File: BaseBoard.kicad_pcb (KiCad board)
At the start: 2 copper layers, 80 parts, among them U1 TLC5971PWP, U10 TLC5971PWP, U11 TLC5971PWP, U12 TLC5971PWP, U13 TLC5971PWP, U14 TLC5971PWP, U15 TLC5971PWP, U16 TLC5971PWP, U2 TLC5971PWP, U3 TLC5971PWP, U4 TLC5971PWP, U5 TLC5971PWP, U6 TLC5971PWP, U7 TLC5971PWP, U8 TLC5971PWP, U9 TLC5971PWP

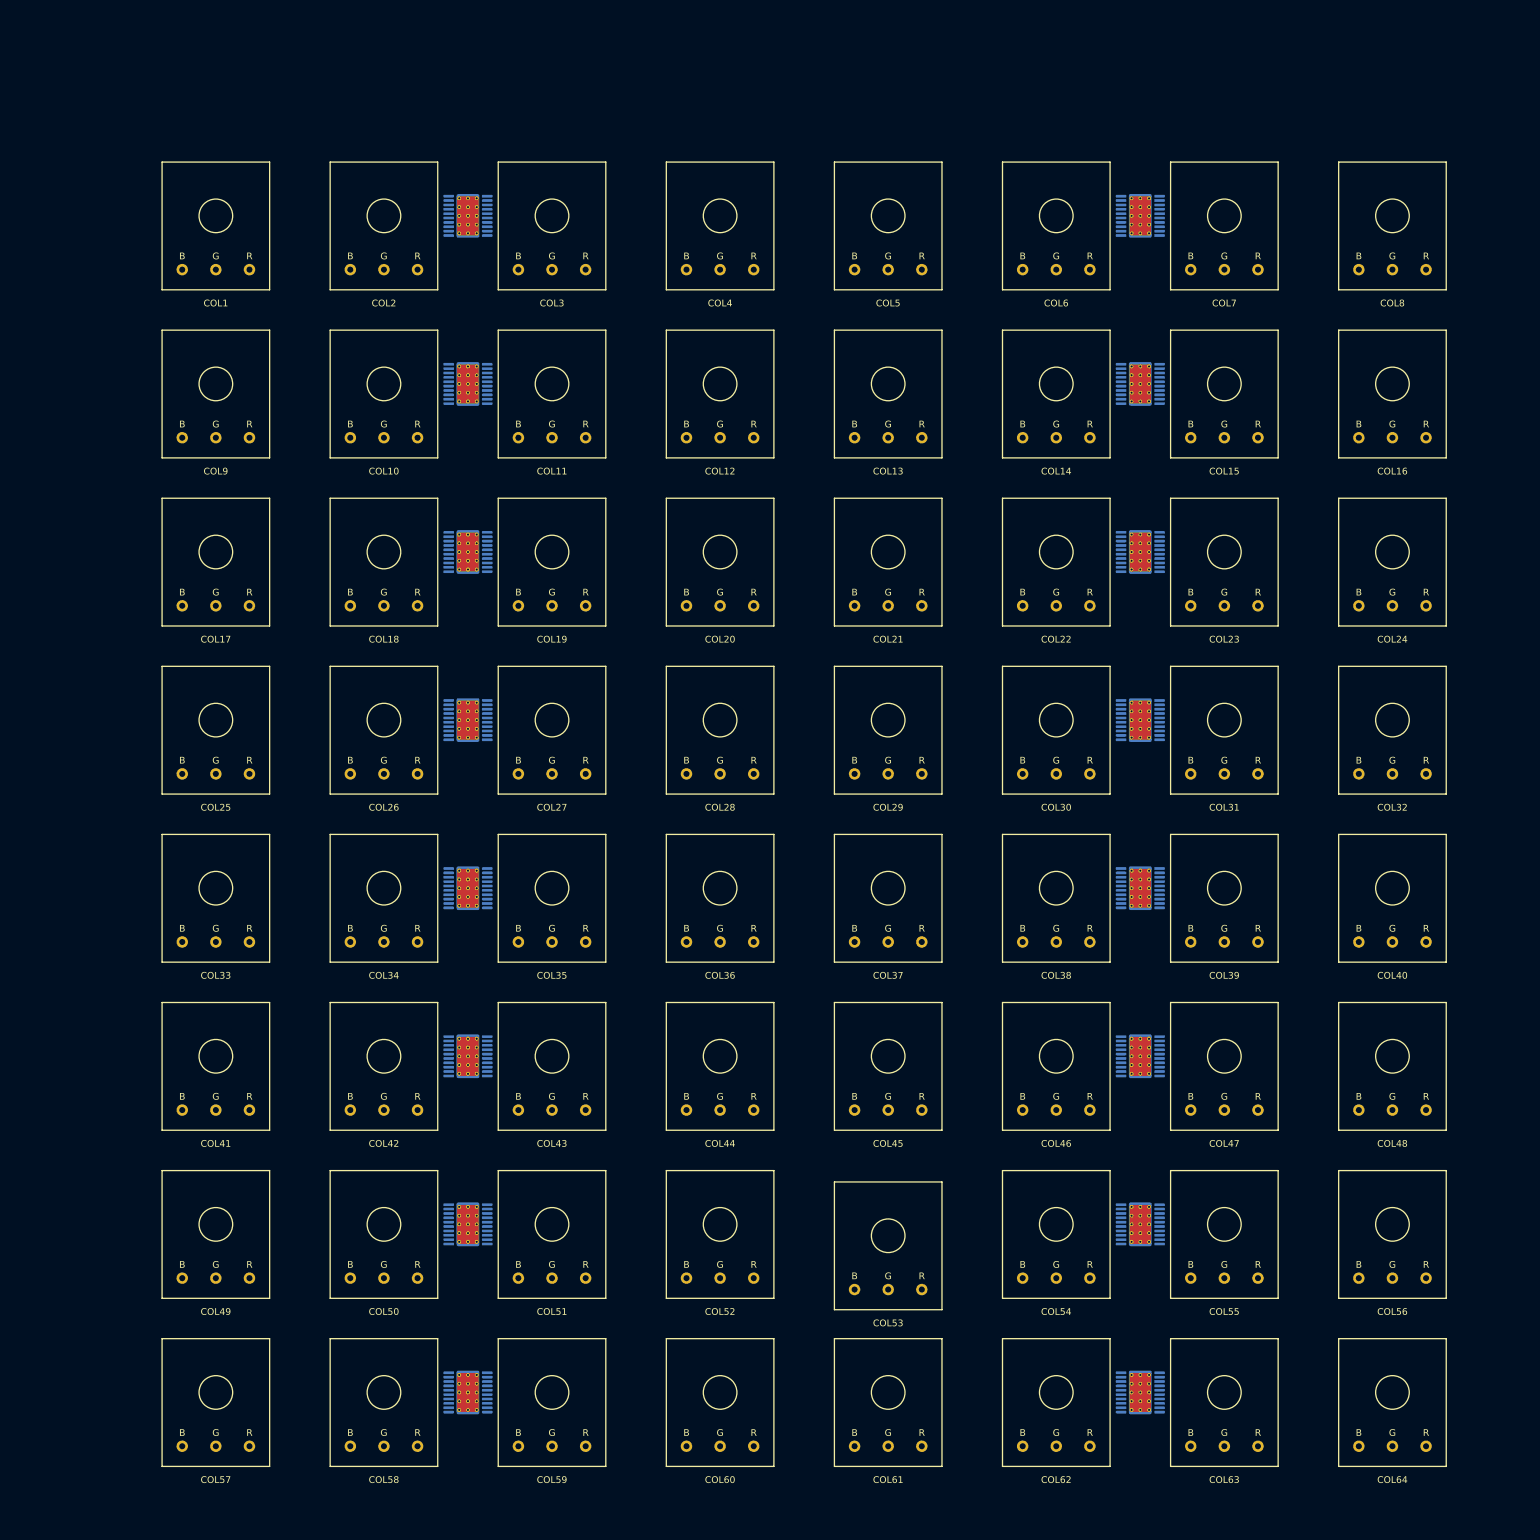
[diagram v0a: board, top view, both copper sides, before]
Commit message: Add PCB base
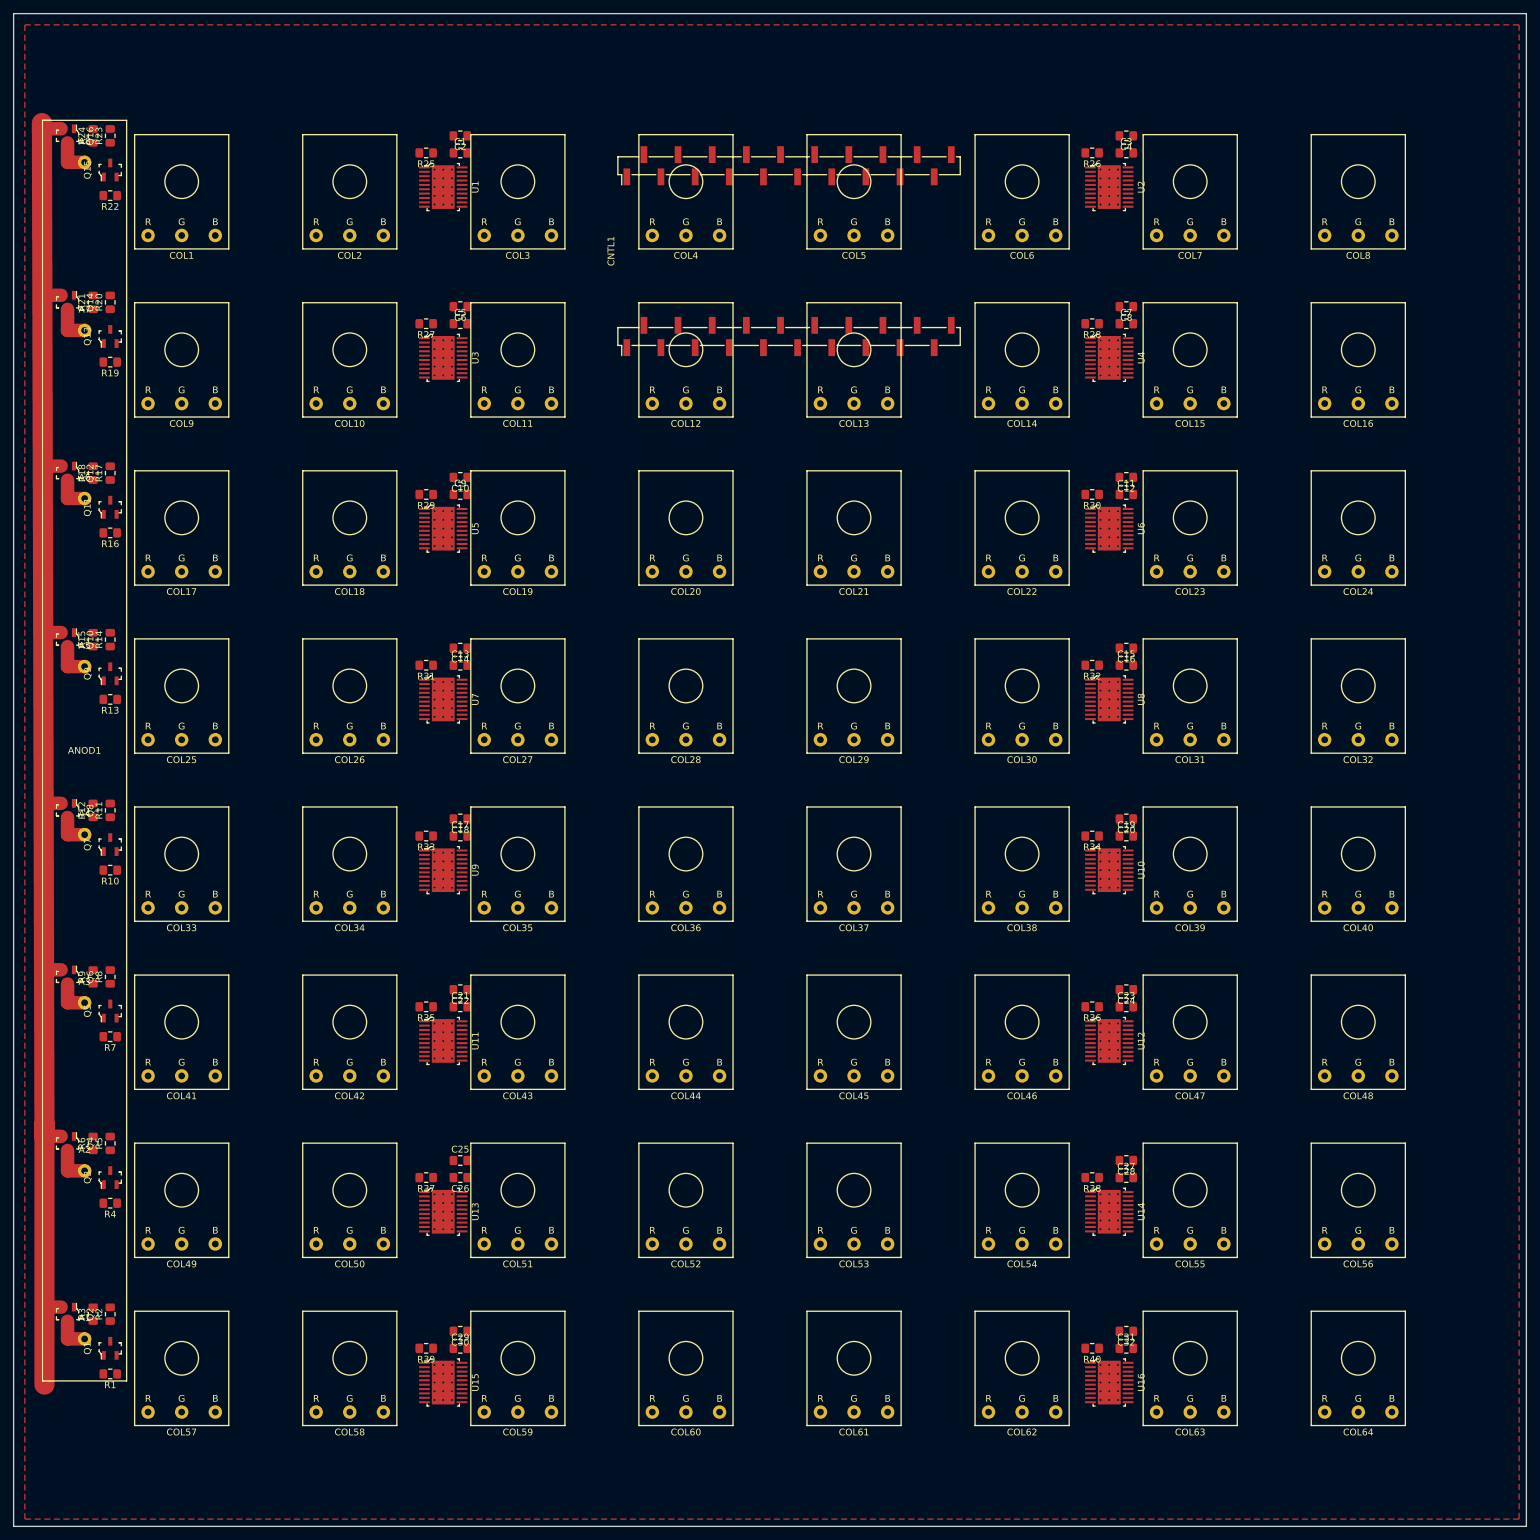
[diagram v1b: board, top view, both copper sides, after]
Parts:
- added ANOD1: Anodes, BaseBoard:Anodes, F.Cu at (30.5, 129.5)
- added C1: 1uF, Capacitor_SMD:C_0805_2012Metric_Pad1.15x1.40mm_HandSolder, F.Cu at (86.4, 40.6)
- added C10: 1uF, Capacitor_SMD:C_0805_2012Metric_Pad1.15x1.40mm_HandSolder, F.Cu at (86.4, 88.9)
- added C11: 1uF, Capacitor_SMD:C_0805_2012Metric_Pad1.15x1.40mm_HandSolder, F.Cu at (185.4, 91.4)
- added C12: 1uF, Capacitor_SMD:C_0805_2012Metric_Pad1.15x1.40mm_HandSolder, F.Cu at (185.4, 88.9)
- added C13: 1uF, Capacitor_SMD:C_0805_2012Metric_Pad1.15x1.40mm_HandSolder, F.Cu at (86.4, 116.8)
- added C14: 1uF, Capacitor_SMD:C_0805_2012Metric_Pad1.15x1.40mm_HandSolder, F.Cu at (86.4, 114.3)
- added C15: 1uF, Capacitor_SMD:C_0805_2012Metric_Pad1.15x1.40mm_HandSolder, F.Cu at (185.4, 116.8)
- added C16: 1uF, Capacitor_SMD:C_0805_2012Metric_Pad1.15x1.40mm_HandSolder, F.Cu at (185.4, 114.3)
- added C17: 1uF, Capacitor_SMD:C_0805_2012Metric_Pad1.15x1.40mm_HandSolder, F.Cu at (86.4, 142.2)
- added C18: 1uF, Capacitor_SMD:C_0805_2012Metric_Pad1.15x1.40mm_HandSolder, F.Cu at (86.4, 139.7)
- added C19: 1uF, Capacitor_SMD:C_0805_2012Metric_Pad1.15x1.40mm_HandSolder, F.Cu at (185.4, 142.2)
- added C2: 1uF, Capacitor_SMD:C_0805_2012Metric_Pad1.15x1.40mm_HandSolder, F.Cu at (86.4, 38.1)
- added C20: 1uF, Capacitor_SMD:C_0805_2012Metric_Pad1.15x1.40mm_HandSolder, F.Cu at (185.4, 139.7)
- added C21: 1uF, Capacitor_SMD:C_0805_2012Metric_Pad1.15x1.40mm_HandSolder, F.Cu at (86.4, 167.6)
- added C22: 1uF, Capacitor_SMD:C_0805_2012Metric_Pad1.15x1.40mm_HandSolder, F.Cu at (86.4, 165.1)
- added C23: 1uF, Capacitor_SMD:C_0805_2012Metric_Pad1.15x1.40mm_HandSolder, F.Cu at (185.4, 167.6)
- added C24: 1uF, Capacitor_SMD:C_0805_2012Metric_Pad1.15x1.40mm_HandSolder, F.Cu at (185.4, 165.1)
- added C25: 1uF, Capacitor_SMD:C_0805_2012Metric_Pad1.15x1.40mm_HandSolder, F.Cu at (86.4, 190.5)
- added C26: 1uF, Capacitor_SMD:C_0805_2012Metric_Pad1.15x1.40mm_HandSolder, F.Cu at (86.4, 193.0)
- added C27: 1uF, Capacitor_SMD:C_0805_2012Metric_Pad1.15x1.40mm_HandSolder, F.Cu at (185.4, 193.0)
- added C28: 1uF, Capacitor_SMD:C_0805_2012Metric_Pad1.15x1.40mm_HandSolder, F.Cu at (185.4, 190.5)
- added C29: 1uF, Capacitor_SMD:C_0805_2012Metric_Pad1.15x1.40mm_HandSolder, F.Cu at (86.4, 218.4)
- added C3: 1uF, Capacitor_SMD:C_0805_2012Metric_Pad1.15x1.40mm_HandSolder, F.Cu at (185.4, 40.6)
- added C30: 1uF, Capacitor_SMD:C_0805_2012Metric_Pad1.15x1.40mm_HandSolder, F.Cu at (86.4, 215.9)
- added C31: 1uF, Capacitor_SMD:C_0805_2012Metric_Pad1.15x1.40mm_HandSolder, F.Cu at (185.4, 218.4)
- added C32: 1uF, Capacitor_SMD:C_0805_2012Metric_Pad1.15x1.40mm_HandSolder, F.Cu at (185.4, 215.9)
- added C4: 1uF, Capacitor_SMD:C_0805_2012Metric_Pad1.15x1.40mm_HandSolder, F.Cu at (185.4, 38.1)
- added C5: 1uF, Capacitor_SMD:C_0805_2012Metric_Pad1.15x1.40mm_HandSolder, F.Cu at (86.4, 66.0)
- added C6: 1uF, Capacitor_SMD:C_0805_2012Metric_Pad1.15x1.40mm_HandSolder, F.Cu at (86.4, 63.5)
- added C7: 1uF, Capacitor_SMD:C_0805_2012Metric_Pad1.15x1.40mm_HandSolder, F.Cu at (185.4, 66.0)
- added C8: 1uF, Capacitor_SMD:C_0805_2012Metric_Pad1.15x1.40mm_HandSolder, F.Cu at (185.4, 63.5)
- added C9: 1uF, Capacitor_SMD:C_0805_2012Metric_Pad1.15x1.40mm_HandSolder, F.Cu at (86.4, 91.4)
- added CNTL1: ESP32_NodeMCU, BaseBoard:ESP32_NodeMCU, F.Cu at (135.3, 55.2)
- added Q1: MMBT2222A-7-F, digikey-footprints:SOT-23-3, F.Cu at (34.3, 218.4)
- added Q10: IRLML6401TRPBF, digikey-footprints:SOT-23-3, F.Cu at (27.9, 113.0)
- added Q11: MMBT2222A-7-F, digikey-footprints:SOT-23-3, F.Cu at (34.3, 93.3)
- added Q12: IRLML6401TRPBF, digikey-footprints:SOT-23-3, F.Cu at (27.9, 88.3)
- added Q13: MMBT2222A-7-F, digikey-footprints:SOT-23-3, F.Cu at (34.3, 67.9)
- added Q14: IRLML6401TRPBF, digikey-footprints:SOT-23-3, F.Cu at (27.9, 62.9)
- added Q15: MMBT2222A-7-F, digikey-footprints:SOT-23-3, F.Cu at (34.3, 43.2)
- added Q16: IRLML6401TRPBF, digikey-footprints:SOT-23-3, F.Cu at (27.9, 38.1)
- added Q2: IRLML6401TRPBF, digikey-footprints:SOT-23-3, F.Cu at (27.9, 213.4)
- added Q3: MMBT2222A-7-F, digikey-footprints:SOT-23-3, F.Cu at (34.3, 193.0)
- added Q4: IRLML6401TRPBF, digikey-footprints:SOT-23-3, F.Cu at (27.9, 188.0)
- added Q5: MMBT2222A-7-F, digikey-footprints:SOT-23-3, F.Cu at (34.3, 168.3)
- added Q6: IRLML6401TRPBF, digikey-footprints:SOT-23-3, F.Cu at (27.9, 163.2)
- added Q7: MMBT2222A-7-F, digikey-footprints:SOT-23-3, F.Cu at (34.3, 143.5)
- added Q8: IRLML6401TRPBF, digikey-footprints:SOT-23-3, F.Cu at (27.9, 138.4)
- added Q9: MMBT2222A-7-F, digikey-footprints:SOT-23-3, F.Cu at (34.3, 118.1)
- added R1: 1K, Resistor_SMD:R_0805_2012Metric_Pad1.15x1.40mm_HandSolder, F.Cu at (34.3, 222.2)
- added R10: 1K, Resistor_SMD:R_0805_2012Metric_Pad1.15x1.40mm_HandSolder, F.Cu at (34.3, 147.3)
- added R11: 1K, Resistor_SMD:R_0805_2012Metric_Pad1.15x1.40mm_HandSolder, F.Cu at (34.3, 138.4)
- added R12: 10, Resistor_SMD:R_0805_2012Metric_Pad1.15x1.40mm_HandSolder, F.Cu at (31.8, 138.4)
- added R13: 1K, Resistor_SMD:R_0805_2012Metric_Pad1.15x1.40mm_HandSolder, F.Cu at (34.3, 121.9)
- added R14: 1K, Resistor_SMD:R_0805_2012Metric_Pad1.15x1.40mm_HandSolder, F.Cu at (34.3, 113.0)
- added R15: 10, Resistor_SMD:R_0805_2012Metric_Pad1.15x1.40mm_HandSolder, F.Cu at (31.8, 113.0)
- added R16: 1K, Resistor_SMD:R_0805_2012Metric_Pad1.15x1.40mm_HandSolder, F.Cu at (34.3, 97.2)
- added R17: 1K, Resistor_SMD:R_0805_2012Metric_Pad1.15x1.40mm_HandSolder, F.Cu at (34.3, 88.3)
- added R18: 10, Resistor_SMD:R_0805_2012Metric_Pad1.15x1.40mm_HandSolder, F.Cu at (31.8, 88.3)
- added R19: 1K, Resistor_SMD:R_0805_2012Metric_Pad1.15x1.40mm_HandSolder, F.Cu at (34.3, 71.8)
- added R2: 1K, Resistor_SMD:R_0805_2012Metric_Pad1.15x1.40mm_HandSolder, F.Cu at (34.3, 213.4)
- added R20: 1K, Resistor_SMD:R_0805_2012Metric_Pad1.15x1.40mm_HandSolder, F.Cu at (34.3, 62.9)
- added R21: 10, Resistor_SMD:R_0805_2012Metric_Pad1.15x1.40mm_HandSolder, F.Cu at (31.8, 62.9)
- added R22: 1K, Resistor_SMD:R_0805_2012Metric_Pad1.15x1.40mm_HandSolder, F.Cu at (34.3, 47.0)
- added R23: 1K, Resistor_SMD:R_0805_2012Metric_Pad1.15x1.40mm_HandSolder, F.Cu at (34.3, 38.1)
- added R24: 10, Resistor_SMD:R_0805_2012Metric_Pad1.15x1.40mm_HandSolder, F.Cu at (31.8, 38.1)
- added R25: 3.3K, Resistor_SMD:R_0805_2012Metric_Pad1.15x1.40mm_HandSolder, F.Cu at (81.3, 40.6)
- added R26: 3.3K, Resistor_SMD:R_0805_2012Metric_Pad1.15x1.40mm_HandSolder, F.Cu at (180.3, 40.6)
- added R27: 3.3K, Resistor_SMD:R_0805_2012Metric_Pad1.15x1.40mm_HandSolder, F.Cu at (81.3, 66.0)
- added R28: 3.3K, Resistor_SMD:R_0805_2012Metric_Pad1.15x1.40mm_HandSolder, F.Cu at (180.3, 66.0)
- added R29: 3.3K, Resistor_SMD:R_0805_2012Metric_Pad1.15x1.40mm_HandSolder, F.Cu at (81.3, 91.4)
- added R3: 10, Resistor_SMD:R_0805_2012Metric_Pad1.15x1.40mm_HandSolder, F.Cu at (31.8, 213.4)
- added R30: 3.3K, Resistor_SMD:R_0805_2012Metric_Pad1.15x1.40mm_HandSolder, F.Cu at (180.3, 91.4)
- added R31: 3.3K, Resistor_SMD:R_0805_2012Metric_Pad1.15x1.40mm_HandSolder, F.Cu at (81.3, 116.8)
- added R32: 3.3K, Resistor_SMD:R_0805_2012Metric_Pad1.15x1.40mm_HandSolder, F.Cu at (180.3, 116.8)
- added R33: 3.3K, Resistor_SMD:R_0805_2012Metric_Pad1.15x1.40mm_HandSolder, F.Cu at (81.3, 142.2)
- added R34: 3.3K, Resistor_SMD:R_0805_2012Metric_Pad1.15x1.40mm_HandSolder, F.Cu at (180.3, 142.2)
- added R35: 3.3K, Resistor_SMD:R_0805_2012Metric_Pad1.15x1.40mm_HandSolder, F.Cu at (81.3, 167.6)
- added R36: 3.3K, Resistor_SMD:R_0805_2012Metric_Pad1.15x1.40mm_HandSolder, F.Cu at (180.3, 167.6)
- added R37: 3.3K, Resistor_SMD:R_0805_2012Metric_Pad1.15x1.40mm_HandSolder, F.Cu at (81.3, 193.0)
- added R38: 3.3K, Resistor_SMD:R_0805_2012Metric_Pad1.15x1.40mm_HandSolder, F.Cu at (180.3, 193.0)
- added R39: 3.3K, Resistor_SMD:R_0805_2012Metric_Pad1.15x1.40mm_HandSolder, F.Cu at (81.3, 218.4)
- added R4: 1K, Resistor_SMD:R_0805_2012Metric_Pad1.15x1.40mm_HandSolder, F.Cu at (34.3, 196.8)
- added R40: 3.3K, Resistor_SMD:R_0805_2012Metric_Pad1.15x1.40mm_HandSolder, F.Cu at (180.3, 218.4)
- added R5: 1K, Resistor_SMD:R_0805_2012Metric_Pad1.15x1.40mm_HandSolder, F.Cu at (34.3, 188.0)
- added R6: 10, Resistor_SMD:R_0805_2012Metric_Pad1.15x1.40mm_HandSolder, F.Cu at (31.8, 188.0)
- added R7: 1K, Resistor_SMD:R_0805_2012Metric_Pad1.15x1.40mm_HandSolder, F.Cu at (34.3, 172.1)
- added R8: 1K, Resistor_SMD:R_0805_2012Metric_Pad1.15x1.40mm_HandSolder, F.Cu at (34.3, 163.2)
- added R9: 10, Resistor_SMD:R_0805_2012Metric_Pad1.15x1.40mm_HandSolder, F.Cu at (31.8, 163.2)
- U1, U10, U11, U12, U13, U14, U15, U16, U2, U3, U4, U5, U6, U7, U8, U9: value TLC5971PWP -> TLC5971PWPR; footprint Package_SO:HTSSOP-20-1EP_4.4x6.5mm_P0.65mm_EP3.4x6.5mm_Mask2.75x3.43mm_ThermalVias -> digikey-footprints:TSSOP-20-1EP_W4.4mm; moved to F.Cu
- moved COL53 8.47 mm to (144.9, 194.9)
- moved COL37 7.18 mm to (144.9, 144.9)
- moved COL38 7.18 mm to (169.9, 144.9)
- moved COL39 7.18 mm to (194.9, 144.9)
- moved COL40 7.18 mm to (219.9, 144.9)
- moved COL45 7.18 mm to (144.9, 169.9)
- moved COL46 7.18 mm to (169.9, 169.9)
- moved COL47 7.18 mm to (194.9, 169.9)
- moved COL48 7.18 mm to (219.9, 169.9)
- moved COL54 7.18 mm to (169.9, 194.9)
- moved COL55 7.18 mm to (194.9, 194.9)
- moved COL56 7.18 mm to (219.9, 194.9)
- moved COL61 7.18 mm to (144.9, 219.9)
- moved COL62 7.18 mm to (169.9, 219.9)
- moved COL63 7.18 mm to (194.9, 219.9)
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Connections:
- U1 pad 19: Net-(U1-Pad19) -> VCC
- U10 pad 19: Net-(U10-Pad19) -> VCC
- U11 pad 19: Net-(U11-Pad19) -> VCC
- U12 pad 19: Net-(U12-Pad19) -> VCC
- U12 pad 2: Net-(U12-Pad2) -> GND
- U12 pad 21: Net-(U12-Pad2) -> GND
- U13 pad 19: Net-(U13-Pad19) -> VCC
- U14 pad 19: Net-(U14-Pad19) -> VCC
- U15 pad 19: Net-(U15-Pad19) -> VCC
- U16 pad 19: Net-(U16-Pad19) -> VCC
- U2 pad 19: Net-(U2-Pad19) -> VCC
- U3 pad 19: Net-(U3-Pad19) -> VCC
- U4 pad 19: Net-(U4-Pad19) -> VCC
- U5 pad 19: Net-(U5-Pad19) -> VCC
- U6 pad 19: Net-(U6-Pad19) -> VCC
- U7 pad 19: Net-(U7-Pad19) -> VCC
- U8 pad 19: Net-(U8-Pad19) -> VCC
- U9 pad 19: Net-(U9-Pad19) -> VCC
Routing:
- net VCC: track 0.00 -> 210.8 mm
- net Net-(ANOD1-Pad7): track 0.00 -> 5.67 mm
- net Net-(ANOD1-Pad2): track 0.00 -> 5.57 mm
- net Net-(ANOD1-Pad5): track 0.00 -> 5.50 mm
- net Net-(ANOD1-Pad8): track 0.00 -> 5.43 mm
- net Net-(ANOD1-Pad3): track 0.00 -> 5.33 mm
- net Net-(ANOD1-Pad6): track 0.00 -> 5.27 mm
- net Net-(ANOD1-Pad1): track 0.00 -> 5.26 mm
- net Net-(ANOD1-Pad4): track 0.00 -> 5.12 mm
- added copper zone on F.Cu, net GND
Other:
- board outline added: 225 x 225 mm

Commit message: Before autorouting
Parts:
- moved CNTL1 3.70 mm to (132.1, 53.3)
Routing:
- net VCC: track 210.8 -> 211.3 mm
